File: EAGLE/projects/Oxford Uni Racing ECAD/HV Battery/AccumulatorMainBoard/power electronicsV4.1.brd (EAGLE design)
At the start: 167.6 x 103.8 mm, 97 parts, among them IC1 4043D, IC2 SE555D, IC3 4011D, IC5 4043D, IC6 4011D, IC7 4011D, IC8 4011D, IC9 4011D, K1 T9AS1D12-48=T9A, K2 T9AS5D12-12=T9A, K3 T9AS1D12-48=T9A, K4 T9AS1D12-48=T9A, Q1 BSS138, Q2 BSS138, Q3 BSS138, Q4 BSS138

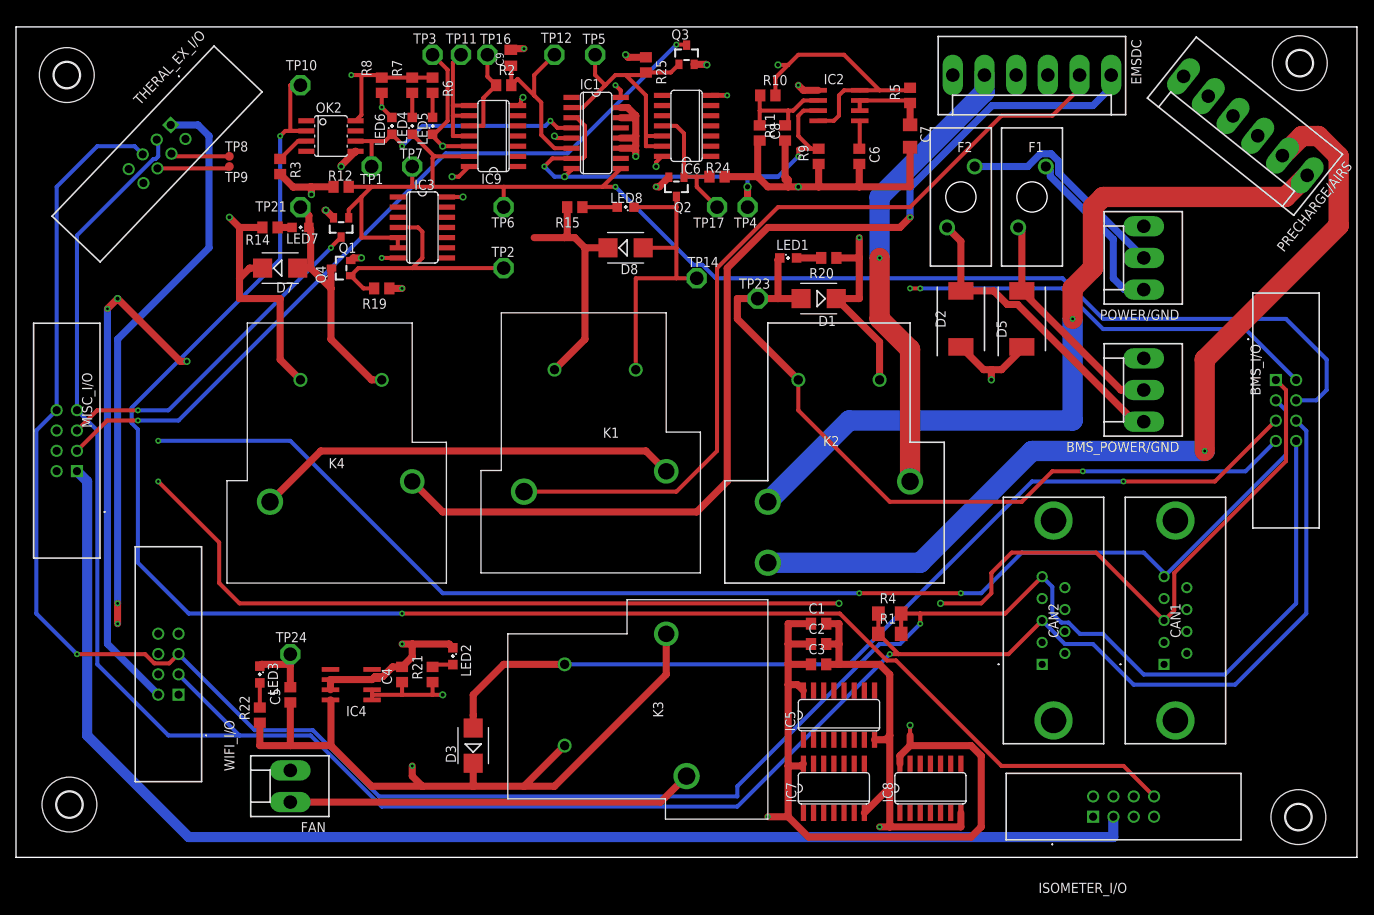
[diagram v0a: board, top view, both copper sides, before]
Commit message: Main Board V4.1
Moves some of the IC to the bottom layer. More optimal Connector placement
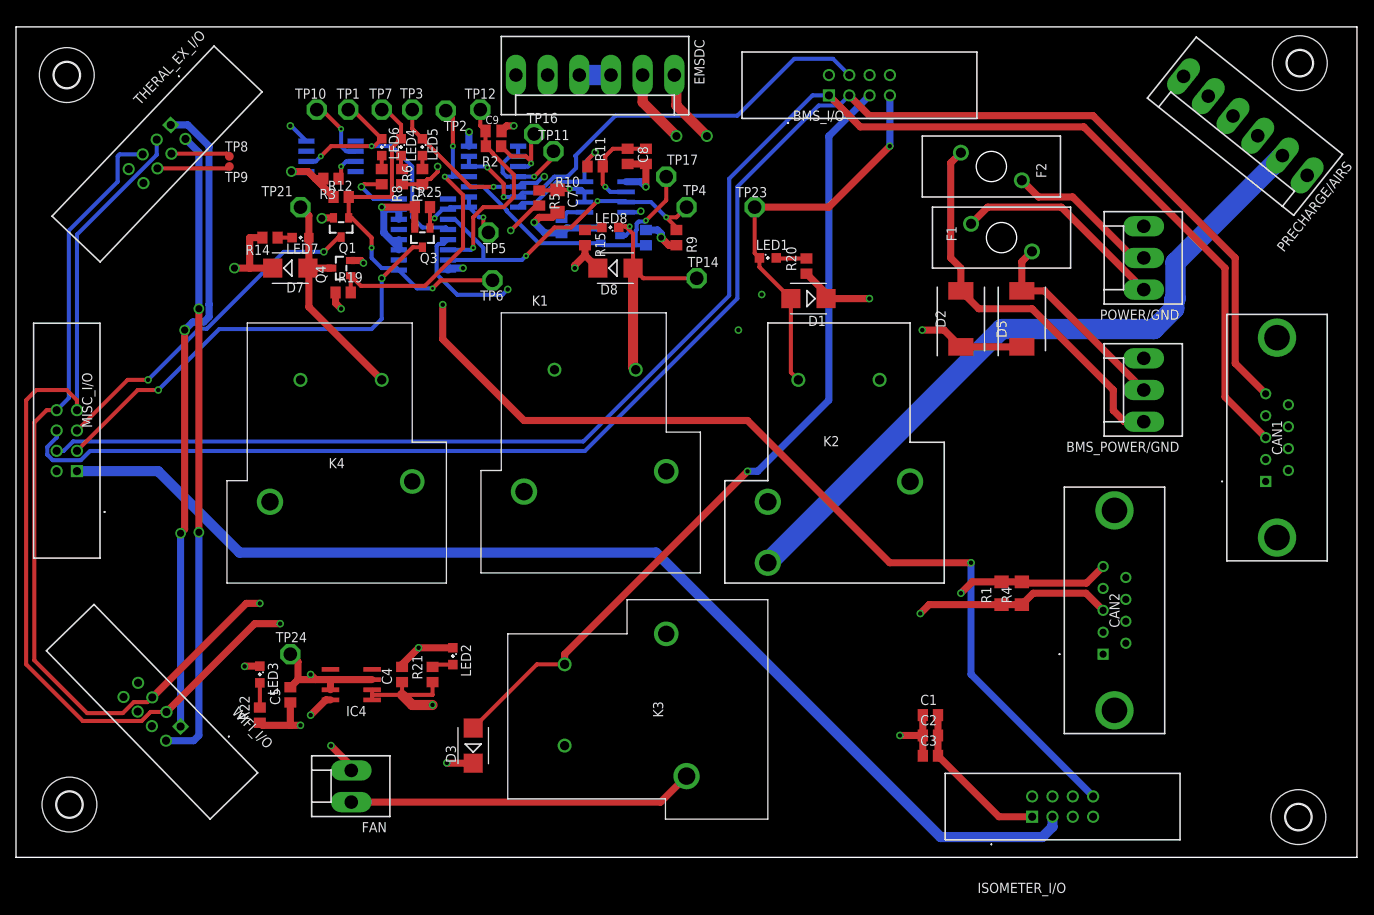
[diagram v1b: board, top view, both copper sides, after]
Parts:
- removed IC3, IC6, IC7, IC8: 4011D, 40xx:SO14
- removed IC5: 4043D, 40xx:SO16
- moved BMS_I/O 68.2 mm to (96.5, 95.2), turned to 0 degrees
- moved EMSDC 54.6 mm to (72.4, 97.8)
- moved R5 48.1 mm to (65.4, 82.4), turned to 270 degrees
- moved C7 44.8 mm to (67.7, 82.0)
- moved Q3 40.2 mm to (50.8, 77.5), turned to 180 degrees
- moved C6 38.2 mm to (68.2, 79.0), flipped to the bottom
- moved R25 33.1 mm to (50.8, 81.3), turned to 0 degrees
- moved IC2 31.4 mm to (73.7, 82.5), flipped to the bottom
- moved CAN1 26.2 mm to (156.2, 47.0)
- moved TP5 25.9 mm to (59.1, 78.1)
- moved IC1 25.0 mm to (50.9, 77.9), flipped to the bottom
- moved R10 23.3 mm to (72.4, 86.4), turned to 180 degrees
- moved TP2 21.0 mm to (53.7, 93.3)
- moved R9 20.5 mm to (82.5, 77.5)
- moved C1 18.1 mm to (114.3, 17.8)
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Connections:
- removed net VDD: IC1.16, IC3.14, IC6.14, IC9.14
- removed net VSS: IC1.8, IC3.7, IC6.7, IC9.7
- net +3V3: now also IC1.16, IC9.14; no longer IC5.16, IC7.14, IC8.14
- net DISCHARGE_ENABLE: now also IC9.5, IC9.6; no longer IC3.5, IC3.6
- net GND: now also IC1.8, IC9.7; no longer IC5.8, IC7.7, IC8.7
- net N$16: now also IC9.4; no longer IC3.4
- net N$8: now also IC9.3; no longer IC6.11
- net N$9: now also IC9.1, IC9.2; no longer IC6.12, IC6.13
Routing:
- net +12V: track 191.9 -> 53.4 mm, vias 4 -> 7
- net VSS: track 89.6 -> 0.00 mm, vias 4 -> 0
- net VDD: track 88.1 -> 0.00 mm, vias 4 -> 0
- net CHARGE_SAFE: track 139.0 -> 64.3 mm, vias 3 -> 2
- net DISCHARGE_ENABLE: track 175.7 -> 115.6 mm, vias 1 -> 4
- net OK_HS: track 213.0 -> 153.0 mm, vias 2 -> 3
- net GND: track 168.3 -> 113.0 mm, vias 14 -> 15
- net N$11: track 97.2 -> 150.6 mm, vias 1 -> 0
- net +3V3: track 180.9 -> 128.8 mm, vias 6 -> 9
- net N$13: track 130.6 -> 81.8 mm
- net PRECHARGE_SELECT: track 97.8 -> 50.3 mm
- net N$14: track 105.4 -> 61.7 mm, vias 0 -> 1
- net IMD_LED-: track 97.3 -> 56.7 mm
- net CAN2_L: track 284.4 -> 321.0 mm
- net CHARGE_POWER: track 250.3 -> 214.4 mm
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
